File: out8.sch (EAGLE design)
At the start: 30 parts, among them IC104 74HC594N, K301 S202S02, K302 S202S02, K303 S202S02, K304 S202S02, K305 S202S02, K306 S202S02, K307 S202S02, K308 S202S02

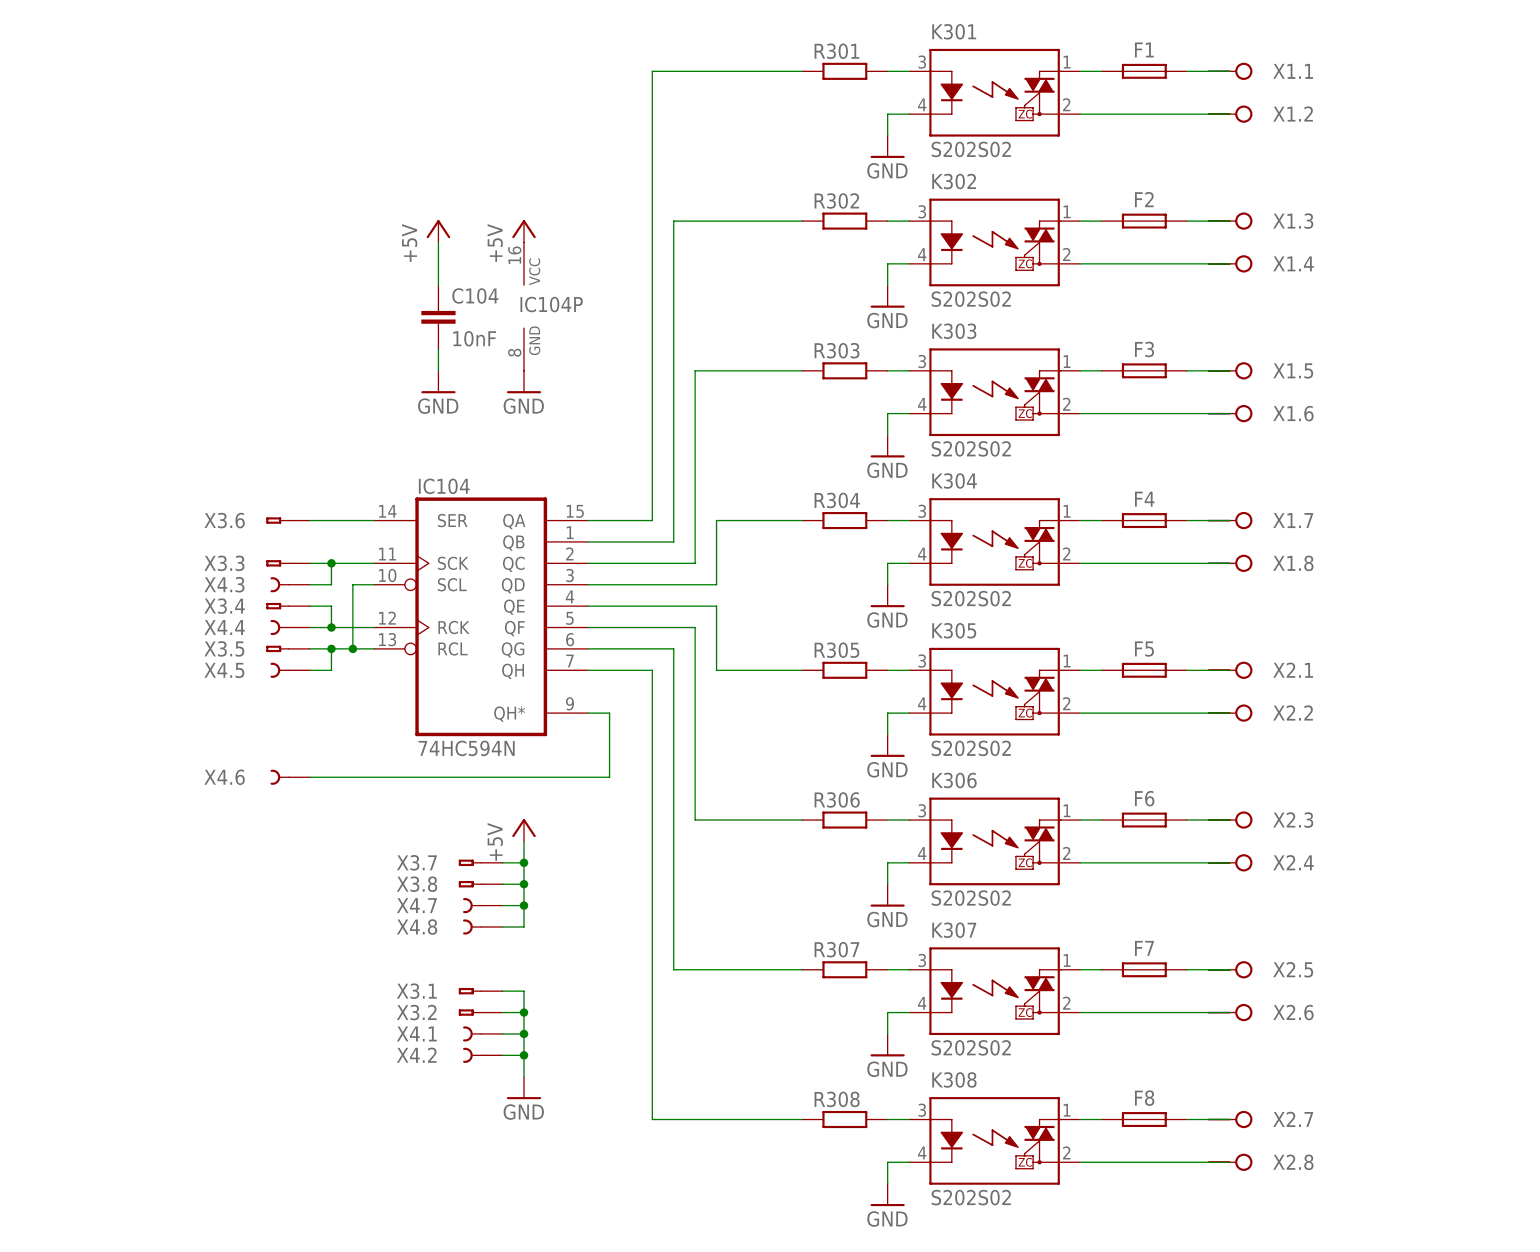
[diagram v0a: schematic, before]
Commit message: LEDs auf Ausgangsplatine hinzugefügt
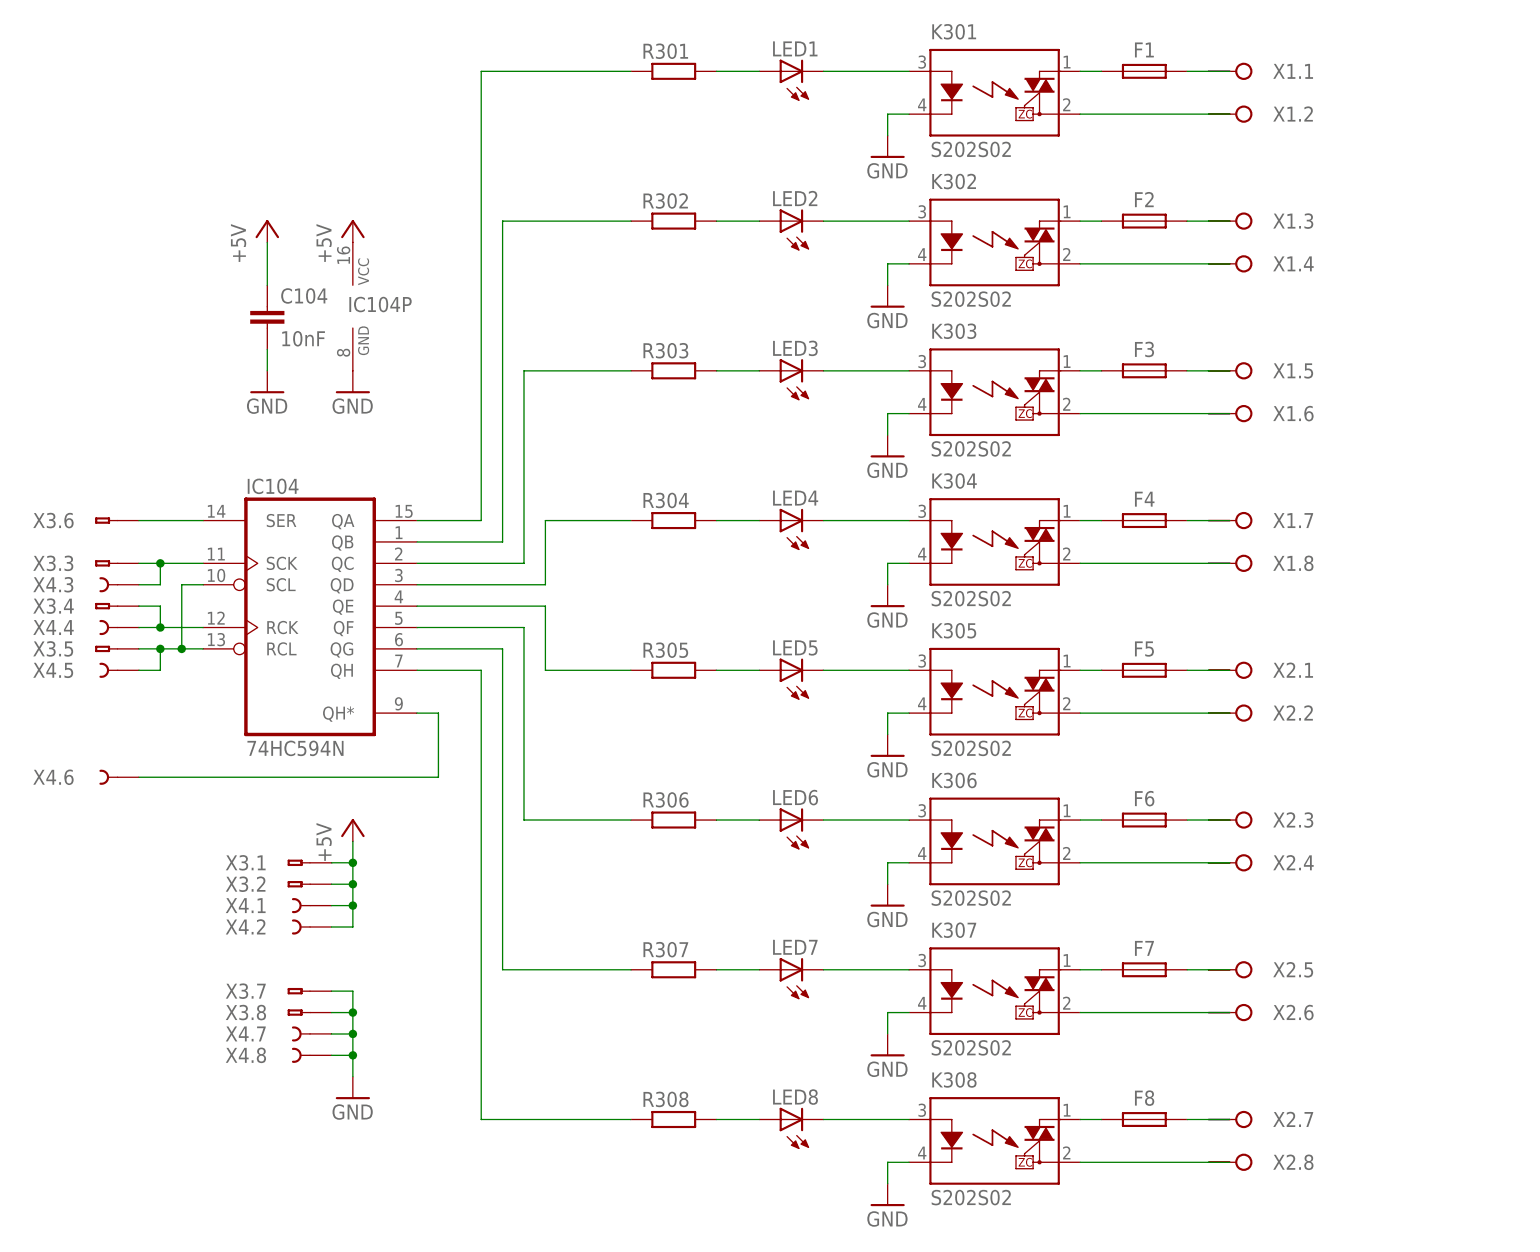
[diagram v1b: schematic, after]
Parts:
- added LED1, LED2, LED3, LED4, LED5, LED6, LED7, LED8: (no value), led:LED3MM
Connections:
- new net N$42: LED1.A, R301.2
- new net N$43: LED2.A, R302.2
- new net N$44: LED3.A, R303.2
- new net N$45: LED4.A, R304.2
- new net N$46: LED5.A, R305.2
- new net N$47: LED6.A, R306.2
- new net N$48: LED7.A, R307.2
- new net N$49: LED8.A, R308.2
- net +5V: now also X3.1.A, X3.2.A, X4.1.A, X4.2.A; no longer X3.7.A, X3.8.A, X4.7.A, X4.8.A
- net GND: now also X3.7.A, X3.8.A, X4.7.A, X4.8.A; no longer X3.1.A, X3.2.A, X4.1.A, X4.2.A
- net N$17: now also LED1.C; no longer R301.2
- net N$18: now also LED2.C; no longer R302.2
- net N$19: now also LED3.C; no longer R303.2
- net N$20: now also LED4.C; no longer R304.2
- net N$21: now also LED5.C; no longer R305.2
- net N$22: now also LED6.C; no longer R306.2
- net N$23: now also LED7.C; no longer R307.2
- net N$24: now also LED8.C; no longer R308.2
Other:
- moved on the sheet: C104, IC104, IC104P, R301, R302, R303, R304, R305, R306, R307, R308, X3.1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

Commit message: Busstecker auf Ausgangsboard ersetzt; kleinere Layoutanpassungen
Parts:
- removed C104: 10nF, passiv:C_025-025X050
- removed IC104: 74HC594N, 74xx-eu:74HC594N
- removed X3: (no value), anschluss:ST8
- removed X4: (no value), anschluss:BU8
- added C101: 10nF, passiv:C_025-025X050
- added IC101: 74HC594N, 74xx-eu:74HC594N
- added X101, X102: (no value), anschluss:WS16V
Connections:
- net !R: now also IC101A.RCL, IC101A.SCL, X101.10.A, X101.9.A, X102.10.A, X102.9.A; no longer IC104A.RCL, IC104A.SCL, X3.5.A, X4.5.A
- net +5V: now also C101.1, IC101P.VCC, X101.1.A, X101.2.A, X101.3.A, X101.4.A, X102.1.A, X102.2.A, X102.3.A, X102.4.A; no longer C104.1, IC104P.VCC, X3.1.A, X3.2.A, X4.1.A, X4.2.A
- net C1: now also IC101A.SCK, X101.5.A, X101.6.A, X102.5.A, X102.6.A; no longer IC104A.SCK, X3.3.A, X4.3.A
- net C2: now also IC101A.RCK, X101.7.A, X101.8.A, X102.7.A, X102.8.A; no longer IC104A.RCK, X3.4.A, X4.4.A
- net D: now also IC101A.SER, X101.11.A, X101.12.A; no longer IC104A.SER, X3.6.A
- net GND: now also C101.2, IC101P.GND, X101.13.A, X101.14.A, X101.15.A, X101.16.A, X102.13.A, X102.14.A, X102.15.A, X102.16.A; no longer C104.2, IC104P.GND, X3.7.A, X3.8.A, X4.7.A, X4.8.A
- net N$1: now also IC101A.QA; no longer IC104A.QA
- net N$2: now also IC101A.QB; no longer IC104A.QB
- net N$3: now also IC101A.QC; no longer IC104A.QC
- net N$4: now also IC101A.QD; no longer IC104A.QD
- net N$41: now also IC101A.QH*, X102.11.A, X102.12.A; no longer IC104A.QH*, X4.6.A
- net N$5: now also IC101A.QE; no longer IC104A.QE
- net N$6: now also IC101A.QF; no longer IC104A.QF
- net N$7: now also IC101A.QG; no longer IC104A.QG
- net N$8: now also IC101A.QH; no longer IC104A.QH
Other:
- moved on the sheet: F1, F2, F3, F4, F5, F6, F7, F8, K301, K302, K303, K304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

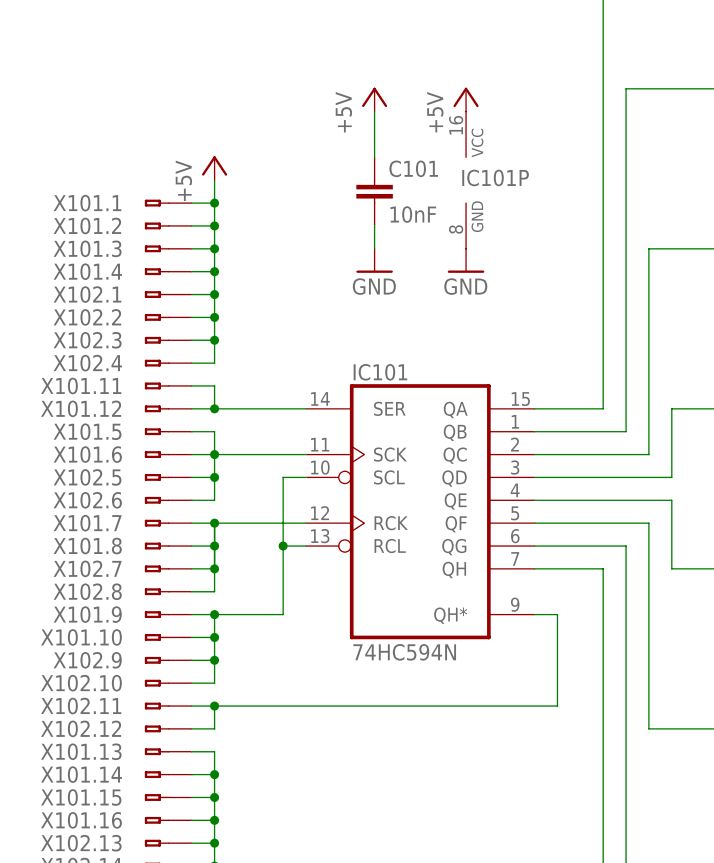
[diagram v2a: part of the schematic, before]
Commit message: Dipschalter durch Drehschalter ersetzt; 74HC594 durch 74HC595 ersetzt; Signalleitungen gedreht.
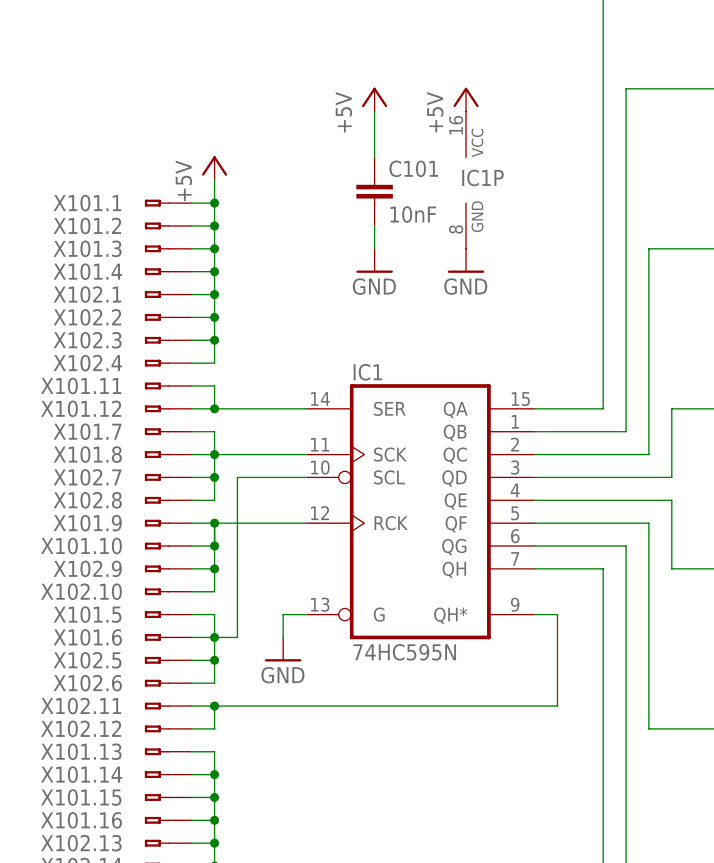
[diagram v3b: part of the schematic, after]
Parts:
- removed IC101: 74HC594N, 74xx-eu:74HC594N
- added IC1: 74HC595N, 74xx-eu:74HC595N
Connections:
- net !R: now also IC1A.SCL, X101.5.A, X101.6.A, X102.5.A, X102.6.A; no longer IC101A.RCL, IC101A.SCL, X101.10.A, X101.9.A, X102.10.A, X102.9.A
- net +5V: now also IC1P.VCC; no longer IC101P.VCC
- net C1: now also IC1A.SCK, X101.7.A, X101.8.A, X102.7.A, X102.8.A; no longer IC101A.SCK, X101.5.A, X101.6.A, X102.5.A, X102.6.A
- net C2: now also IC1A.RCK, X101.10.A, X101.9.A, X102.10.A, X102.9.A; no longer IC101A.RCK, X101.7.A, X101.8.A, X102.7.A, X102.8.A
- net D: now also IC1A.SER; no longer IC101A.SER
- net GND: now also IC1A.G, IC1P.GND; no longer IC101P.GND
- net N$1: now also IC1A.QA; no longer IC101A.QA
- net N$2: now also IC1A.QB; no longer IC101A.QB
- net N$3: now also IC1A.QC; no longer IC101A.QC
- net N$4: now also IC1A.QD; no longer IC101A.QD
- net N$41: now also IC1A.QH*; no longer IC101A.QH*
- net N$5: now also IC1A.QE; no longer IC101A.QE
- net N$6: now also IC1A.QF; no longer IC101A.QF
- net N$7: now also IC1A.QG; no longer IC101A.QG
- net N$8: now also IC1A.QH; no longer IC101A.QH
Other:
- moved on the sheet: X101.10, X101.5, X101.6, X101.7, X101.8, X101.9, X102.10, X102.5, X102.6, X102.7, X102.8, X102.9

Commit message: Werte im Schema und Bohrungen im Layout hinzugefügt
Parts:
- C101: value 10nF -> 100nF
- F1, F2, F3, F4, F5, F6, F7, F8: value (none) -> 2T
- R301, R302, R303, R304, R305, R306, R307, R308: value (none) -> 180Ω
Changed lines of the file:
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@@
 <part name="K307" library="relais" deviceset="S*02S02" device="" technology="2"/>
 <part name="K308" library="relais" deviceset="S*02S02" device="" technology="2"/>
-<part name="R301" library="passiv" deviceset="R_" device="0204/7"/>
-<part name="R302" library="passiv" deviceset="R_" device="0204/7"/>
-<part name="R303" library="passiv" deviceset="R_" device="0204/7"/>
-<part name="R304" library="passiv" deviceset="R_" device="0204/7"/>
-<part name="R305" library="passiv" deviceset="R_" device="0204/7"/>
-<part name="R306" library="passiv" deviceset="R_" device="0204/7"/>
-<part name="R307" library="passiv" deviceset="R_" device="0204/7"/>
-<part name="R308" library="passiv" deviceset="R_" device="0204/7"/>
+<part name="R301" library="passiv" deviceset="R_" device="0204/7" value="180Ω"/>
+<part name="R302" library="passiv" deviceset="R_" device="0204/7" value="180Ω"/>
+<part name="R303" library="passiv" deviceset="R_" device="0204/7" value="180Ω"/>
+<part name="R304" library="passiv" deviceset="R_" device="0204/7" value="180Ω"/>
+<part name="R305" library="passiv" deviceset="R_" device="0204/7" value="180Ω"/>
+<part name="R306" library="passiv" deviceset="R_" device="0204/7" value="180Ω"/>
+<part name="R307" library="passiv" deviceset="R_" device="0204/7" value="180Ω"/>
+<part name="R308" library="passiv" deviceset="R_" device="0204/7" value="180Ω"/>
 <part name="GND9" library="versorgung" deviceset="GND" device=""/>
 <part name="GND10" library="versorgung" deviceset="GND" device=""/>
@@
 <part name="GND15" library="versorgung" deviceset="GND" device=""/>
 <part name="GND16" library="versorgung" deviceset="GND" device=""/>
-<part name="C101" library="passiv" deviceset="C_" device="025-025X050" value="10nF"/>
+<part name="C101" library="passiv" deviceset="C_" device="025-025X050" value="100nF"/>
 <part name="P+6" library="versorgung" deviceset="+5V" device=""/>
 <part name="P+7" library="versorgung" deviceset="+5V" device=""/>
 <part name="GND38" library="versorgung" deviceset="GND" device=""/>
 <part name="GND39" library="versorgung" deviceset="GND" device=""/>
-<part name="F1" library="sicherung" deviceset="TR5" device=""/>
-<part name="F2" library="sicherung" deviceset="TR5" device=""/>
-<part name="F3" library="sicherung" deviceset="TR5" device=""/>
-<part name="F4" library="sicherung" deviceset="TR5" device=""/>
-<part name="F5" library="sicherung" deviceset="TR5" device=""/>
-<part name="F6" library="sicherung" deviceset="TR5" device=""/>
-<part name="F7" library="sicherung" deviceset="TR5" device=""/>
-<part name="F8" library="sicherung" deviceset="TR5" device=""/>
+<part name="F1" library="sicherung" deviceset="TR5" device="" value="2T"/>
+<part name="F2" library="sicherung" deviceset="TR5" device="" value="2T"/>
+<part name="F3" library="sicherung" deviceset="TR5" device="" value="2T"/>
+<part name="F4" library="sicherung" deviceset="TR5" device="" value="2T"/>
+<part name="F5" library="sicherung" deviceset="TR5" device="" value="2T"/>
+<part name="F6" library="sicherung" deviceset="TR5" device="" value="2T"/>
+<part name="F7" library="sicherung" deviceset="TR5" device="" value="2T"/>
+<part name="F8" library="sicherung" deviceset="TR5" device="" value="2T"/>
 <part name="X1" library="anschluss" deviceset="WAGO_236-408" device=""/>
 <part name="X2" library="anschluss" deviceset="WAGO_236-408" device=""/>
